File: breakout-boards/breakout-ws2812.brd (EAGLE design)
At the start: 21.6 x 14 mm, 7 parts

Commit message: Schönheitskorrekturen
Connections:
- net JDD renamed VDD
- net N$3 renamed VCC
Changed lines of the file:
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@@
 <setting verticaltext="up"/>
 </settings>
-<grid distance="0.05" unitdist="inch" unit="inch" style="lines" multiple="1" display="yes" altdistance="0.025" altunitdist="inch" altunit="inch"/>
+<grid distance="50" unitdist="mil" unit="mil" style="lines" multiple="1" display="yes" altdistance="25" altunitdist="mil" altunit="mil"/>
 <layers>
 <layer number="1" name="Top" color="4" fill="1" visible="yes" active="yes"/>
@@
 <text x="14.605" y="11.049" size="1.016" layer="16" font="vector" ratio="15" rot="MR0">Netz39 e.V.</text>
 <text x="13.716" y="1.778" size="1.016" layer="16" font="vector" ratio="15" rot="MR0">CC-BY-SA</text>
-<text x="19.685" y="0.762" size="1.27" layer="16" font="vector" rot="MR0">+</text>
-<text x="19.685" y="12.065" size="1.27" layer="16" font="vector" rot="MR0">G</text>
-<text x="0.254" y="0.381" size="1.27" layer="16" font="vector" rot="MR0">O</text>
-<text x="-0.127" y="12.192" size="1.27" layer="16" font="vector" rot="MR0">I</text>
+<text x="19.685" y="0.762" size="1.27" layer="16" font="vector" ratio="15" rot="MR0">+</text>
+<text x="19.685" y="12.065" size="1.27" layer="16" font="vector" ratio="15" rot="MR0">G</text>
+<text x="0.254" y="0.381" size="1.27" layer="16" font="vector" ratio="15" rot="MR0">O</text>
+<text x="-0.127" y="12.192" size="1.27" layer="16" font="vector" ratio="15" rot="MR0">I</text>
 </plain>
 <attributes>
@@
 <signal name="GND">
 <polygon width="0.4064" layer="16">
-<vertex x="0" y="12.7"/>
-<vertex x="19.05" y="12.7"/>
-<vertex x="19.05" y="1.27"/>
-<vertex x="0" y="1.27"/>
+<vertex x="-1.27" y="13.97"/>
+<vertex x="20.32" y="13.97"/>
+<vertex x="20.32" y="0"/>
+<vertex x="-1.27" y="0"/>
 </polygon>
 <contactref element="C1" pad="2"/>
@@
 <contactref element="JGND" pad="1"/>
 </signal>
-<signal name="JDD">
+<signal name="VDD">
 <contactref element="R1" pad="2"/>
 <contactref element="U$1" pad="5"/>
@@
 <wire x1="16.662" y1="3.962" x2="16.662" y2="5.715" width="0.6096" layer="16"/>
 </signal>
-<signal name="N$3">
+<signal name="VCC">
 <contactref element="R1" pad="1"/>
 <contactref element="U$1" pad="3"/>

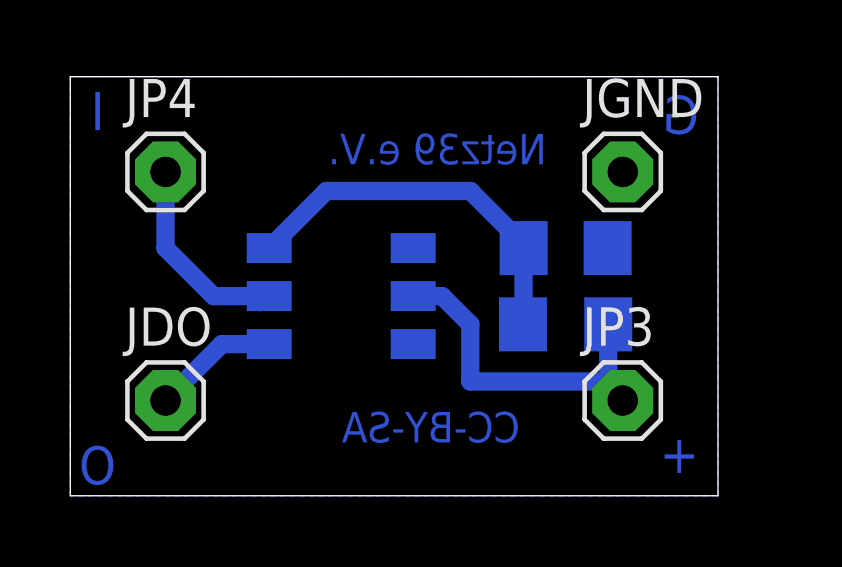
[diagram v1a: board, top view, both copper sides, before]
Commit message: move board dimension to origin, update ws2812 package, reroute
The lower left corner of the board dimension was not coincident with the
coordinates 0,0 which lead to difficulties moving an exported dxf to the
right place for drilling/milling, so I moved everything an half inch to
the right. Then I used the new centered ws2812 package and routed the
wires again. The drills are still in place, but next time the board is
slightly different.
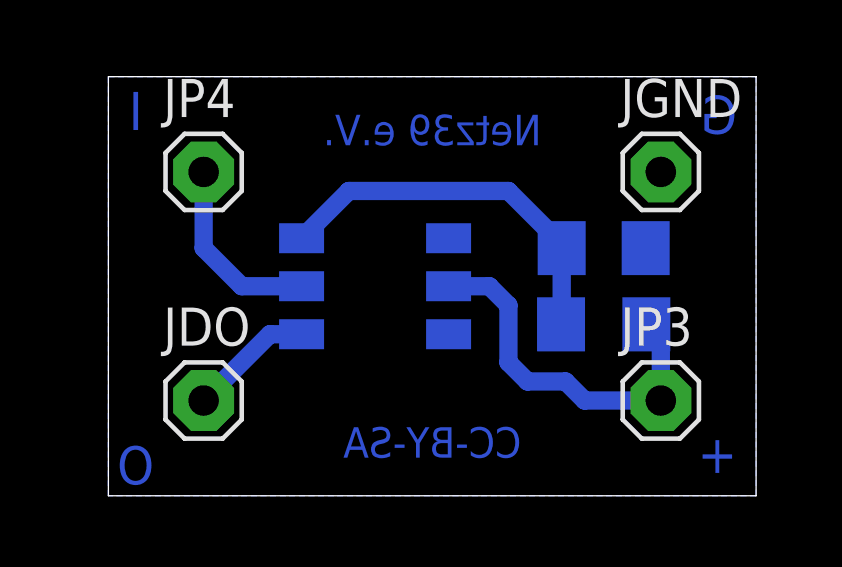
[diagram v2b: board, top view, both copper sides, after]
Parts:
- moved U$1 1.80 mm to (8.89, 6.99)
- moved C1 1.27 mm to (16.5, 8.26)
- moved R1 1.27 mm to (16.5, 5.71)
- moved JDO 1.27 mm to (3.17, 3.17)
- moved JP4 1.27 mm to (3.17, 10.8)
- moved JGND 1.27 mm to (18.4, 10.8)
- moved JP3 1.27 mm to (18.4, 3.17)
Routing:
- net VDD: track 11.5 -> 12.5 mm
- net JDI: track 7.09 -> 6.33 mm
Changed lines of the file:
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@@
 <setting verticaltext="up"/>
 </settings>
-<grid distance="50" unitdist="mil" unit="mil" style="lines" multiple="1" display="yes" altdistance="25" altunitdist="mil" altunit="mil"/>
+<grid distance="25" unitdist="mil" unit="mil" style="lines" multiple="1" display="yes" altdistance="25" altunitdist="mil" altunit="mil"/>
 <layers>
 <layer number="1" name="Top" color="4" fill="1" visible="yes" active="yes"/>
@@
 <layer number="23" name="tOrigins" color="15" fill="1" visible="yes" active="yes"/>
 <layer number="24" name="bOrigins" color="15" fill="1" visible="yes" active="yes"/>
-<layer number="25" name="tNames" color="7" fill="1" visible="yes" active="yes"/>
-<layer number="26" name="bNames" color="7" fill="1" visible="yes" active="yes"/>
-<layer number="27" name="tValues" color="7" fill="1" visible="yes" active="yes"/>
-<layer number="28" name="bValues" color="7" fill="1" visible="yes" active="yes"/>
+<layer number="25" name="tNames" color="7" fill="1" visible="no" active="yes"/>
+<layer number="26" name="bNames" color="7" fill="1" visible="no" active="yes"/>
+<layer number="27" name="tValues" color="7" fill="1" visible="no" active="yes"/>
+<layer number="28" name="bValues" color="7" fill="1" visible="no" active="yes"/>
 <layer number="29" name="tStop" color="7" fill="3" visible="no" active="yes"/>
 <layer number="30" name="bStop" color="7" fill="6" visible="no" active="yes"/>
@@
 <layer number="37" name="tTest" color="7" fill="1" visible="no" active="yes"/>
 <layer number="38" name="bTest" color="7" fill="1" visible="no" active="yes"/>
-<layer number="39" name="tKeepout" color="4" fill="11" visible="yes" active="yes"/>
-<layer number="40" name="bKeepout" color="1" fill="11" visible="yes" active="yes"/>
-<layer number="41" name="tRestrict" color="4" fill="10" visible="yes" active="yes"/>
-<layer number="42" name="bRestrict" color="1" fill="10" visible="yes" active="yes"/>
-<layer number="43" name="vRestrict" color="2" fill="10" visible="yes" active="yes"/>
-<layer number="44" name="Drills" color="7" fill="1" visible="no" active="yes"/>
+<layer number="39" name="tKeepout" color="4" fill="11" visible="no" active="yes"/>
+<layer number="40" name="bKeepout" color="1" fill="11" visible="no" active="yes"/>
+<layer number="41" name="tRestrict" color="4" fill="10" visible="no" active="yes"/>
+<layer number="42" name="bRestrict" color="1" fill="10" visible="no" active="yes"/>
+<layer number="43" name="vRestrict" color="2" fill="10" visible="no" active="yes"/>
+<layer number="44" name="Drills" color="7" fill="1" visible="yes" active="yes"/>
 <layer number="45" name="Holes" color="7" fill="1" visible="no" active="yes"/>
 <layer number="46" name="Milling" color="3" fill="1" visible="no" active="yes"/>
@@
 <board>
 <plain>
-<wire x1="-1.27" y1="0" x2="20.32" y2="0" width="0" layer="20"/>
-<wire x1="20.32" y1="0" x2="20.32" y2="13.97" width="0" layer="20"/>
-<wire x1="20.32" y1="13.97" x2="-1.27" y2="13.97" width="0" layer="20"/>
-<wire x1="-1.27" y1="13.97" x2="-1.27" y2="0" width="0" layer="20"/>
-<text x="14.605" y="11.049" size="1.016" layer="16" font="vector" ratio="15" rot="MR0">Netz39 e.V.</text>
-<text x="13.716" y="1.778" size="1.016" layer="16" font="vector" ratio="15" rot="MR0">CC-BY-SA</text>
-<text x="19.685" y="0.762" size="1.27" layer="16" font="vector" ratio="15" rot="MR0">+</text>
-<text x="19.685" y="12.065" size="1.27" layer="16" font="vector" ratio="15" rot="MR0">G</text>
-<text x="0.254" y="0.381" size="1.27" layer="16" font="vector" ratio="15" rot="MR0">O</text>
-<text x="-0.127" y="12.192" size="1.27" layer="16" font="vector" ratio="15" rot="MR0">I</text>
+<wire x1="0" y1="0" x2="21.59" y2="0" width="0" layer="20"/>
+<wire x1="21.59" y1="0" x2="21.59" y2="13.97" width="0" layer="20"/>
+<wire x1="21.59" y1="13.97" x2="0" y2="13.97" width="0" layer="20"/>
+<wire x1="0" y1="13.97" x2="0" y2="0" width="0" layer="20"/>
+<text x="10.795" y="12.7" size="1.016" layer="16" font="vector" ratio="15" rot="MR0" align="top-center">Netz39 e.V.</text>
+<text x="10.795" y="1.27" size="1.016" layer="16" font="vector" ratio="15" rot="MR0" align="bottom-center">CC-BY-SA</text>
+<text x="20.955" y="0.762" size="1.27" layer="16" font="vector" ratio="15" rot="MR0">+</text>
+<text x="20.955" y="12.065" size="1.27" layer="16" font="vector" ratio="15" rot="MR0">G</text>
+<text x="1.524" y="0.381" size="1.27" layer="16" font="vector" ratio="15" rot="MR0">O</text>
+<text x="1.143" y="12.192" size="1.27" layer="16" font="vector" ratio="15" rot="MR0">I</text>
 </plain>
 <attributes>
@@
 </autorouter>
 <elements>
-<element name="U$1" library="n39" package="WS2812" value="WS2812" x="10.16" y="8.255" rot="MR0"/>
-<element name="R1" library="resistor" package="R1206" value="" x="15.24" y="5.715" rot="MR180"/>
-<element name="C1" library="resistor" package="C1206" value="" x="15.24" y="8.255" rot="MR180"/>
-<element name="JP3" library="pinhead" package="1X01" value="VDD" x="17.145" y="3.175"/>
-<element name="JP4" library="pinhead" package="1X01" value="DI" x="1.905" y="10.795"/>
-<element name="JGND" library="pinhead" package="1X01" value="GND" x="17.145" y="10.795"/>
-<element name="JDO" library="pinhead" package="1X01" value="DO" x="1.905" y="3.175"/>
+<element name="U$1" library="n39" package="WS2812" value="WS2812" x="8.89" y="6.985" rot="MR0"/>
+<element name="R1" library="resistor" package="R1206" value="" x="16.51" y="5.715" rot="MR180"/>
+<element name="C1" library="resistor" package="C1206" value="" x="16.51" y="8.255" rot="MR180"/>
+<element name="JP3" library="pinhead" package="1X01" value="VDD" x="18.415" y="3.175"/>
+<element name="JP4" library="pinhead" package="1X01" value="DI" x="3.175" y="10.795"/>
+<element name="JGND" library="pinhead" package="1X01" value="GND" x="18.415" y="10.795"/>
+<element name="JDO" library="pinhead" package="1X01" value="DO" x="3.175" y="3.175"/>
 </elements>
 <signals>
 <signal name="GND">
 <polygon width="0.4064" layer="16">
-<vertex x="-1.27" y="13.97"/>
-<vertex x="20.32" y="13.97"/>
-<vertex x="20.32" y="0"/>
-<vertex x="-1.27" y="0"/>
+<vertex x="0" y="13.97"/>
+<vertex x="21.59" y="13.97"/>
+<vertex x="21.59" y="0"/>
+<vertex x="0" y="0"/>
 </polygon>
 <contactref element="C1" pad="2"/>
@@
 <contactref element="U$1" pad="5"/>
 <contactref element="JP3" pad="1"/>
-<wire x1="17.145" y1="3.175" x2="16.51" y2="3.81" width="0.6096" layer="16"/>
-<wire x1="16.51" y1="3.81" x2="12.065" y2="3.81" width="0.6096" layer="16"/>
-<wire x1="12.065" y1="3.81" x2="12.065" y2="5.715" width="0.6096" layer="16"/>
-<wire x1="12.065" y1="5.715" x2="11.125" y2="6.655" width="0.6096" layer="16"/>
-<wire x1="11.125" y1="6.655" x2="10.16" y2="6.655" width="0.6096" layer="16"/>
-<wire x1="16.51" y1="3.81" x2="16.662" y2="3.962" width="0.4064" layer="16"/>
-<wire x1="16.662" y1="3.962" x2="16.662" y2="5.715" width="0.6096" layer="16"/>
+<wire x1="11.34" y1="6.985" x2="12.7" y2="6.985" width="0.6096" layer="16"/>
+<wire x1="12.7" y1="6.985" x2="13.335" y2="6.35" width="0.6096" layer="16"/>
+<wire x1="13.335" y1="6.35" x2="13.335" y2="4.445" width="0.6096" layer="16"/>
+<wire x1="13.335" y1="4.445" x2="13.97" y2="3.81" width="0.6096" layer="16"/>
+<wire x1="13.97" y1="3.81" x2="15.24" y2="3.81" width="0.6096" layer="16"/>
+<wire x1="15.24" y1="3.81" x2="15.875" y2="3.175" width="0.6096" layer="16"/>
+<wire x1="15.875" y1="3.175" x2="18.415" y2="3.175" width="0.6096" layer="16"/>
+<wire x1="18.415" y1="3.175" x2="18.415" y2="5.232" width="0.6096" layer="16"/>
+<wire x1="18.415" y1="5.232" x2="17.932" y2="5.715" width="0.6096" layer="16"/>
 </signal>
 <signal name="VCC">
@@
 <contactref element="U$1" pad="3"/>
 <contactref element="C1" pad="1"/>
-<wire x1="13.818" y1="5.715" x2="13.84" y2="5.737" width="0.4064" layer="16"/>
-<wire x1="13.84" y1="5.737" x2="13.84" y2="8.255" width="0.6096" layer="16"/>
-<wire x1="5.36" y1="8.255" x2="7.265" y2="10.16" width="0.6096" layer="16"/>
-<wire x1="7.265" y1="10.16" x2="12.065" y2="10.16" width="0.6096" layer="16"/>
-<wire x1="12.065" y1="10.16" x2="13.84" y2="8.385" width="0.6096" layer="16"/>
-<wire x1="13.84" y1="8.385" x2="13.84" y2="8.255" width="0.4064" layer="16"/>
+<wire x1="15.088" y1="5.715" x2="15.11" y2="5.715" width="0.6096" layer="16"/>
+<wire x1="15.11" y1="5.715" x2="15.11" y2="8.255" width="0.6096" layer="16"/>
+<wire x1="15.11" y1="8.255" x2="15.11" y2="8.385" width="0.6096" layer="16"/>
+<wire x1="15.11" y1="8.385" x2="13.335" y2="10.16" width="0.6096" layer="16"/>
+<wire x1="13.335" y1="10.16" x2="8.015" y2="10.16" width="0.6096" layer="16"/>
+<wire x1="8.015" y1="10.16" x2="6.44" y2="8.585" width="0.6096" layer="16"/>
 </signal>
 <signal name="JDI">
 <contactref element="U$1" pad="2"/>
 <contactref element="JP4" pad="1"/>
-<wire x1="5.36" y1="6.655" x2="5.055" y2="6.35" width="0.4064" layer="16"/>
-<wire x1="1.905" y1="8.255" x2="1.905" y2="10.795" width="0.6096" layer="16"/>
-<wire x1="1.905" y1="8.255" x2="3.505" y2="6.655" width="0.6096" layer="16"/>
-<wire x1="3.505" y1="6.655" x2="5.36" y2="6.655" width="0.6096" layer="16"/>
+<wire x1="6.44" y1="6.985" x2="4.445" y2="6.985" width="0.6096" layer="16"/>
+<wire x1="4.445" y1="6.985" x2="3.175" y2="8.255" width="0.6096" layer="16"/>
+<wire x1="3.175" y1="8.255" x2="3.175" y2="10.795" width="0.6096" layer="16"/>
 </signal>
 <signal name="N$2">
 <contactref element="U$1" pad="1"/>
 <contactref element="JDO" pad="1"/>
-<wire x1="1.905" y1="3.175" x2="3.785" y2="5.055" width="0.6096" layer="16"/>
-<wire x1="3.785" y1="5.055" x2="5.36" y2="5.055" width="0.6096" layer="16"/>
+<wire x1="6.44" y1="5.385" x2="5.385" y2="5.385" width="0.6096" layer="16"/>
+<wire x1="5.385" y1="5.385" x2="3.175" y2="3.175" width="0.6096" layer="16"/>
 </signal>
 </signals>
